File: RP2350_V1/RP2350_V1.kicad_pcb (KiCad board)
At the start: 4 copper layers, 72 parts, among them J1 Conn_01x04_Pin, J2 Conn_01x08_Socket, J3 USB_C_Receptacle_USB2.0_16P, J4 Conn_01x08_Socket, J5 Conn_01x08_Socket, J6 Conn_01x02_Pin, SW1 PTS 647 SN50 SMTR2 LFS, SW10 PTS 647 SN50 SMTR2 LFS, SW11 PTS 647 SN50 SMTR2 LFS, SW12 PTS 647 SN50 SMTR2 LFS, SW13 PTS 647 SN50 SMTR2 LFS, SW14 PTS 647 SN50 SMTR2 LFS, SW4 PTS 647 SN50 SMTR2 LFS, SW9 PTS 647 SN50 SMTR2 LFS, U1 RP2350_60QFN, U2 W25Q128JVS, U4 MCP73812T-420I-OT, U6 74HC14, Y1 ASE-12.000MHZ-ET

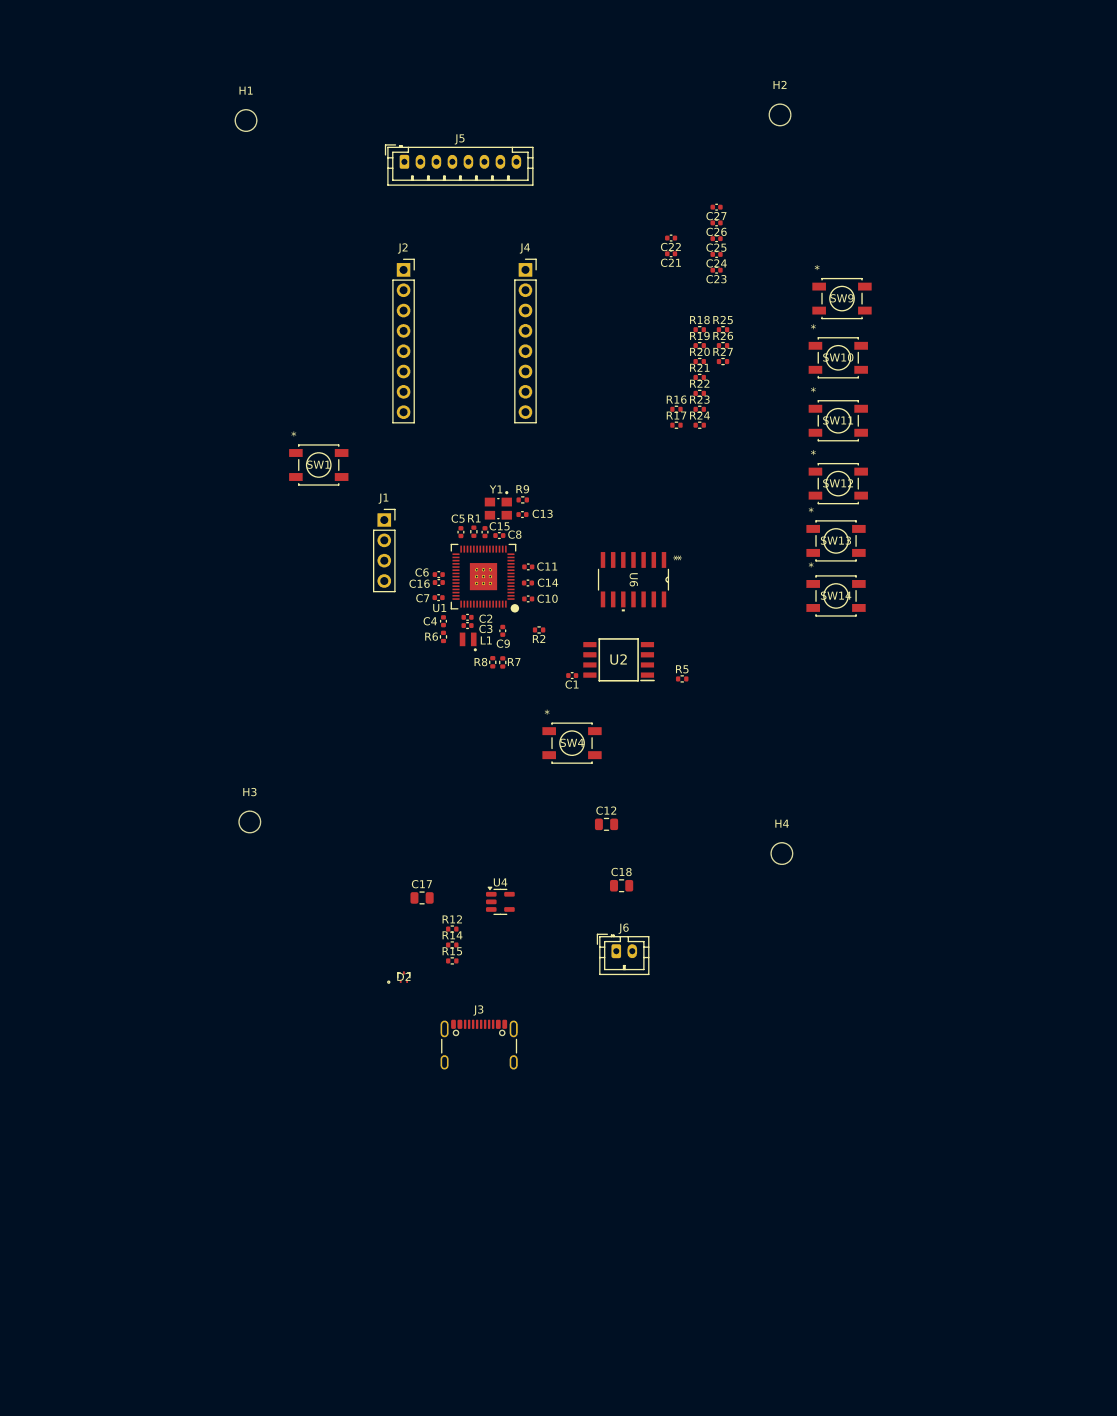
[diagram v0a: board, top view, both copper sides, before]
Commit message: First pass routing done! MCU pin updates. UVLO Reset resistor update
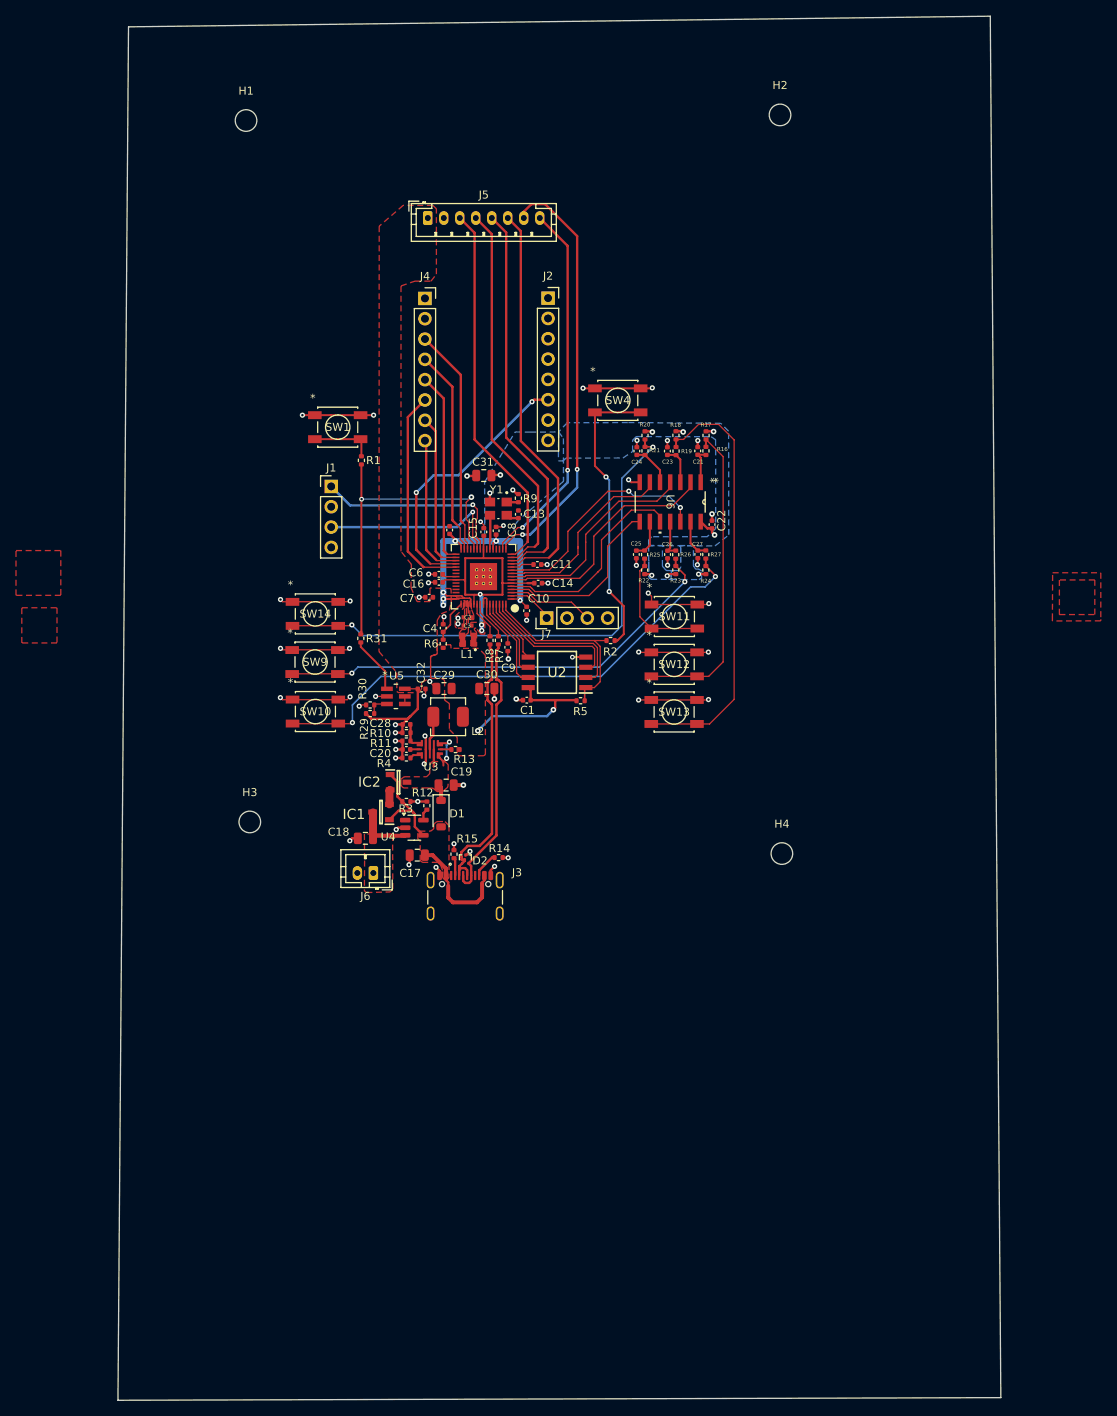
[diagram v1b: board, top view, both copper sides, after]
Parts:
- removed C12: 10u, Capacitor_SMD:C_0805_2012Metric
- added C19: 22u, Capacitor_SMD:C_0805_2012Metric, F.Cu at (140.1, 108.6)
- added C20: 4.7n, Capacitor_SMD:C_0402_1005Metric, F.Cu at (135.2, 104.2)
- added C28: 10p, Capacitor_SMD:C_0402_1005Metric, F.Cu at (135.2, 101.1)
- added C29: 10u, Capacitor_SMD:C_0805_2012Metric, F.Cu at (139.9, 96.6)
- added C30: 22u, Capacitor_SMD:C_0805_2012Metric, F.Cu at (145.2, 96.6)
- added C31: 22u, Capacitor_SMD:C_0805_2012Metric, F.Cu at (144.8, 70.0)
- added C32: 0.1u, Capacitor_SMD:C_0402_1005Metric, F.Cu at (137.1, 96.6)
- added D1: MBR0520LT, Diode_SMD:D_SOD-123, F.Cu at (139.5, 112.2)
- added IC1: DMP1045U-7, My_Footprints:SOT96P240X110-3N, F.Cu at (132.0, 112.0)
- added IC2: DMP1045U-7, My_Footprints:SOT96P240X110-3N, F.Cu at (134.2, 108.3)
- added J7: Conn_01x04_Pin, Connector_PinHeader_2.54mm:PinHeader_1x04_P2.54mm_Vertical, F.Cu at (152.7, 87.8)
- added L2: 0.47u, Inductor_SMD:L_Changjiang_FXL0420, F.Cu at (140.4, 100.1)
- added R10: 88.7k, Resistor_SMD:R_0402_1005Metric, F.Cu at (135.2, 102.1)
- added R11: 19.6k, Resistor_SMD:R_0402_1005Metric, F.Cu at (135.2, 103.1)
- added R13: 100k, Resistor_SMD:R_0402_1005Metric, F.Cu at (141.3, 104.2)
- added R29: 1.5Meg, Resistor_SMD:R_0402_1005Metric, F.Cu at (130.6, 99.7)
- added R3: 100k, Resistor_SMD:R_0402_1005Metric, F.Cu at (135.2, 110.7)
- added R30: 1Meg, Resistor_SMD:R_0402_1005Metric, F.Cu at (130.7, 98.6)
- added R31: 10k, Resistor_SMD:R_0402_1005Metric, F.Cu at (129.5, 90.3)
- added R4: 8.06k, Resistor_SMD:R_0402_1005Metric, F.Cu at (135.2, 105.2)
- added U3: TPS628110AQWRWYRQ1, My_Footprints:RWY0009A, F.Cu at (138.1, 104.2)
- added U5: TLV3012AIDBVR, My_Footprints:DBV6, F.Cu at (133.9, 97.6)
- C2, C3: footprint Capacitor_SMD:C_0402_1005Metric -> My_Footprints:C_0402_1005Metric_small_pads
- J1: footprint Connector_PinSocket_2.54mm:PinSocket_1x04_P2.54mm_Vertical -> Connector_PinHeader_2.54mm:PinHeader_1x04_P2.54mm_Vertical
- moved SW9 80.0 mm to (123.8, 93.3)
- moved SW10 78.9 mm to (123.8, 99.5)
- moved SW14 65.1 mm to (123.8, 87.2)
- moved C27 43.5 mm to (171.6, 79.8), turned to -90 degrees
- moved SW4 43.2 mm to (161.6, 60.5)
- moved C26 41.9 mm to (167.8, 79.8), turned to -90 degrees
- moved C25 40.7 mm to (163.9, 79.8), turned to -90 degrees
- moved C22 36.2 mm to (173.4, 76.1), turned to -90 degrees
- moved C18 32.6 mm to (130.1, 115.3), turned to 180 degrees
- moved SW11 31.9 mm to (168.7, 87.6)
- moved J6 31.9 mm to (131.0, 119.6), turned to 180 degrees
- moved SW12 30.5 mm to (168.7, 93.5)
- moved R25 29.8 mm to (164.9, 79.8), turned to 90 degrees
- moved SW13 29.4 mm to (168.6, 99.5)
- moved R26 26.8 mm to (168.8, 79.8), turned to 90 degrees
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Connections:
- net Net-(R1-Pad1) renamed /RUN_IN
- D2 pad 1: /USB_D+ -> /USB_D-
- D2 pad 2: /USB_D- -> /USB_D+
- U1 pad 10: unconnected-(U1-GPIO7-Pad10) -> /BTN_MACRO_C
- U1 pad 2: unconnected-(U1-GPIO0-Pad2) -> /UART_Tx_DEBUG
- U1 pad 27: /SPI0_RX -> unconnected-(U1-GPIO16-Pad27)
- U1 pad 3: /BTN_MACRO_A -> /UART_Rx_DEBUG
- U1 pad 35: unconnected-(U1-GPIO23-Pad35) -> /SPI0_RX
- U1 pad 4: /BTN_MACRO_B -> /BTN_MACRO_A
- U1 pad 5: /BTN_BACK -> /BTN_MACRO_B
- U1 pad 7: /BTN_OK -> /BTN_BACK
- U1 pad 8: /BTN_NEXT -> /BTN_OK
- U1 pad 9: /BTN_MACRO_C -> /BTN_NEXT
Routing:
- net GND: track 0.00 -> 118.8 mm, vias 0 -> 60
- net +3V3: track 0.00 -> 99.3 mm, vias 0 -> 19
- net Net-(R20-Pad2): track 0.00 -> 68.4 mm, vias 0 -> 2
- net Net-(R24-Pad2): track 0.00 -> 64.5 mm, vias 0 -> 2
- net Net-(R23-Pad2): track 0.00 -> 57.2 mm, vias 0 -> 2
- net Net-(R18-Pad2): track 0.00 -> 53.9 mm
- net /DISPLAY_RESET: track 0.00 -> 53.4 mm, vias 0 -> 2
- net /DISPLAY_DC: track 0.00 -> 50.6 mm
- net /SPI1_CS: track 0.00 -> 49.4 mm
- net /SPI1_CLK: track 0.00 -> 48.1 mm
- net /SPI1_TX: track 0.00 -> 46.7 mm
- net /DISPLAY_BUSY: track 0.00 -> 46.5 mm, vias 0 -> 2
- net /RUN: track 0.00 -> 41.9 mm, vias 0 -> 2
- net Net-(R16-Pad1): track 0.00 -> 39.3 mm
- net /~{USB_BOOT}: track 0.00 -> 36.4 mm, vias 0 -> 2
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- added copper zone on F.Cu, net +1V1
- added copper zone on B.Cu, net +3V3
- added copper zone on F.Cu, net +3V3
- added copper zone on F.Cu, net /Converter_In
- added copper zone on F.Cu, net /VBAT
- added copper zone on F.Cu, net /VREG_LX
- added copper zone on F.Cu, net GND
- added copper zone on In1.Cu, net GND
- added copper zone on In2.Cu, net GND
- added copper zone on F.Cu, net VBUS
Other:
- board outline added: 110.4 x 173 mm
- rule pad_to_mask_clearance: 0 -> 0.051

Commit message: Added LEDs, edege cuts, silkscreen logo
next steps --> DRC
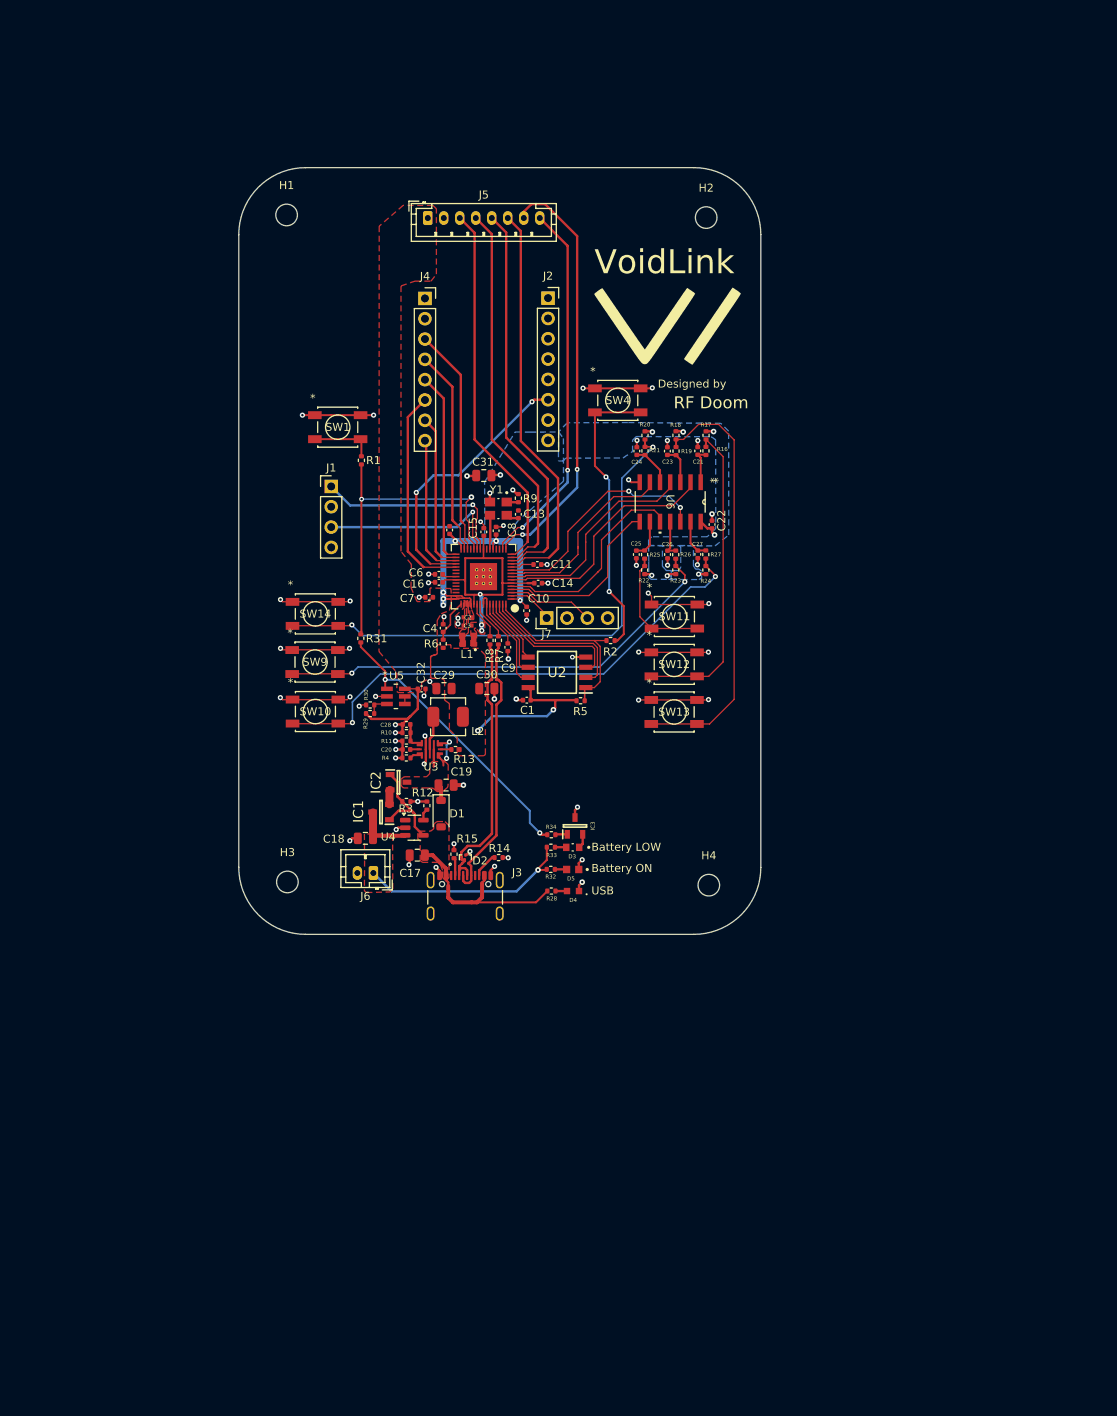
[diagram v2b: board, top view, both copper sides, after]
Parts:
- added D3: LTST-C190KRKT, My_Footprints:LEDC1608X35N_red, F.Cu at (156.0, 116.4)
- added D4: LTST-C190TBKT, My_Footprints:LEDM1608X80_blue, F.Cu at (156.0, 121.9)
- added D5: LTST-C191KFKT, My_Footprints:LEDC1608X55N_orange, F.Cu at (156.0, 119.2)
- added G***: LOGO, LOGO, F.Cu at (167.9, 51.3)
- added IC3: DMP1045U-7, My_Footprints:SOT96P240X110-3N, F.Cu at (156.2, 113.7)
- added R28: 100, Resistor_SMD:R_0402_1005Metric, F.Cu at (153.3, 121.9)
- added R32: 120, Resistor_SMD:R_0402_1005Metric, F.Cu at (153.2, 119.2)
- added R33: 120, Resistor_SMD:R_0402_1005Metric, F.Cu at (153.2, 116.4)
- added R34: 100k, Resistor_SMD:R_0402_1005Metric, F.Cu at (153.3, 114.8)
- moved H2 15.8 mm to (172.7, 37.7)
- moved H1 12.8 mm to (120.2, 37.4)
- moved H4 9.95 mm to (173.0, 121.2)
- moved H3 8.85 mm to (120.3, 120.8)
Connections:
- net Net-(U5-OUT) renamed /UVLO_RST
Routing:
- net /UVLO_RST: track 7.15 -> 36.3 mm, vias 0 -> 2
- net /VBAT: track 7.43 -> 34.5 mm, vias 0 -> 1
- net VBUS: track 27.5 -> 37.6 mm
- net GND: track 118.8 -> 122.9 mm, vias 60 -> 63
- net Net-(IC3-S): track 0.00 -> 1.81 mm
- net Net-(IC3-G): track 0.00 -> 1.51 mm
- net Net-(D5-PadA): track 0.00 -> 1.47 mm
- net Net-(D4-PadA): track 0.00 -> 1.44 mm
- net Net-(D3-PadA): track 0.00 -> 1.42 mm
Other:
- board size 110.4 x 173 mm -> 65.3 x 95.8 mm
- board text added: "Battery LOW"
- board text added: "Battery ON"
- board text added: "Designed by"
- board text added: "RF Doom"
- board text added: "USB"
- board text added: "VoidLink"

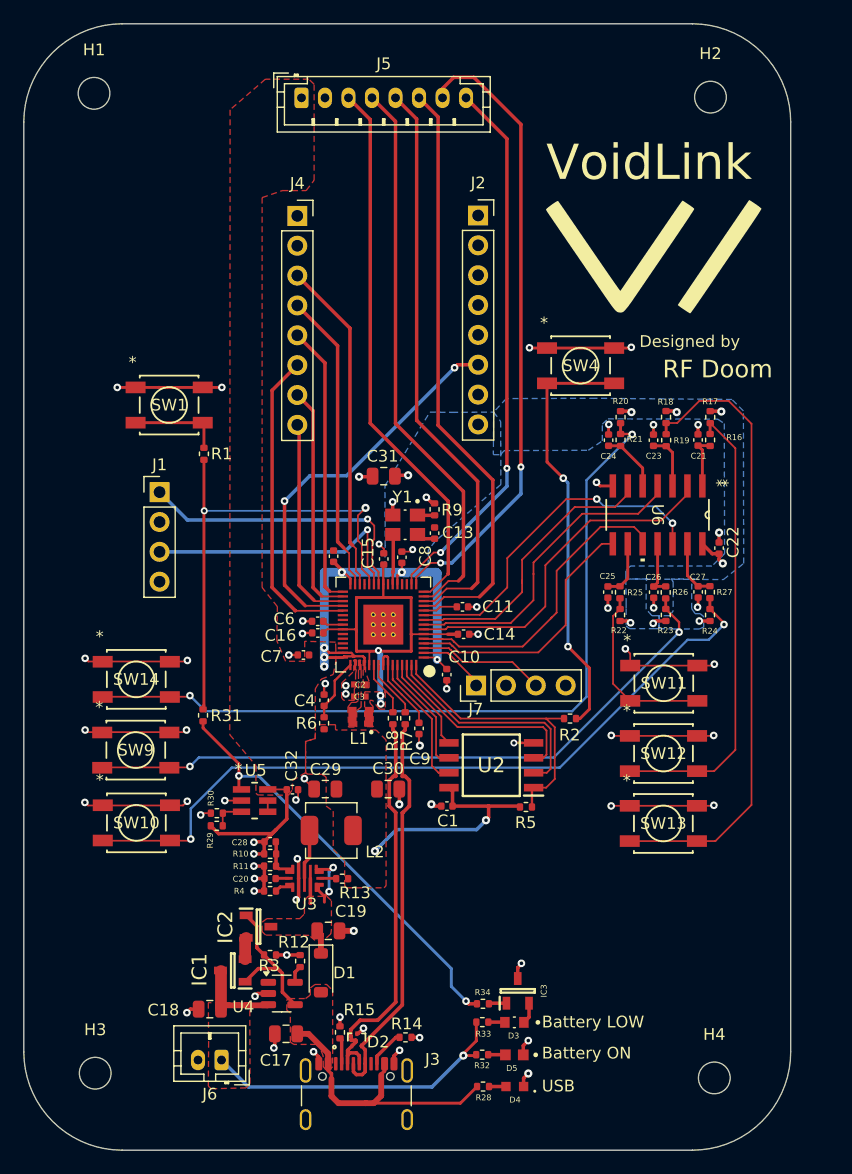
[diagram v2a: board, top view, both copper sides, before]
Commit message: DRC Clean (with waivers)
Added manual vias to RP2350 GND pad.
Silkscreen updates.
Remaining DRCs seem waivable (TPS62811 footprint bug, USB C through holes, RP2350 footprint corners)
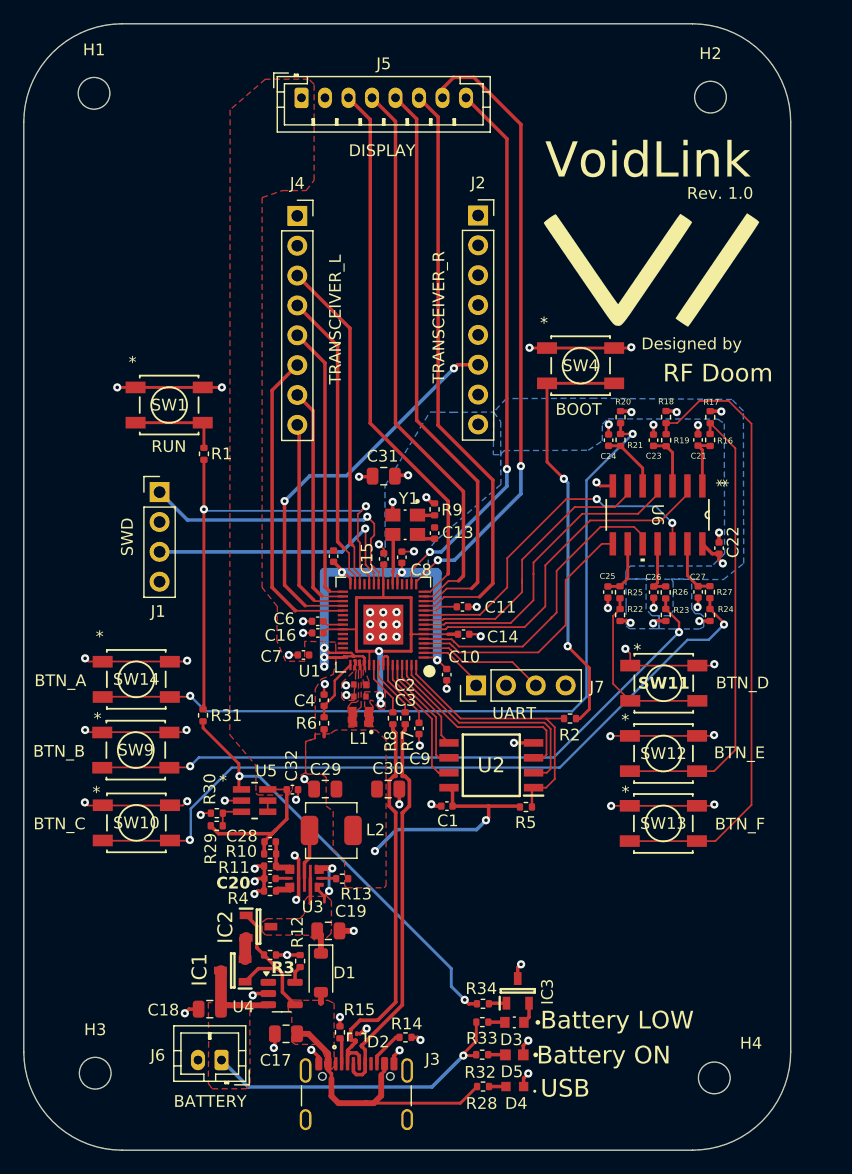
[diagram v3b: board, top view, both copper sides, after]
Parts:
- moved G*** 1.15 mm to (167.7, 52.5)
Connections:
- net Net-(U3-COMP_FSET) renamed /COMP_FSET
- net Net-(U3-FB) renamed /FB
- net Net-(U3-PG) renamed /PG
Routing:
- net GND: track 122.9 -> 124.5 mm, vias 63 -> 72
- net +3V3: track 99.3 -> 98.1 mm, vias 19 -> 17
- net VBUS: track 37.6 -> 38.4 mm
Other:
- board text added: "BATTERY"
- board text added: "BOOT"
- board text added: "BTN_A"
- board text added: "BTN_B"
- board text added: "BTN_C"
- board text added: "BTN_D"
- board text added: "BTN_E"
- board text added: "BTN_F"
- board text added: "DISPLAY"
- board text added: "RUN"
- board text added: "Rev. 1.0"
- board text added: "SWD"
- board text added: "TRANSCEIVER_L"
- board text added: "TRANSCEIVER_R"
- board text added: "UART"
